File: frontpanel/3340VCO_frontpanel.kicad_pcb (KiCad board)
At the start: 2 copper layers, 20 x 128.5 mm, 0 parts

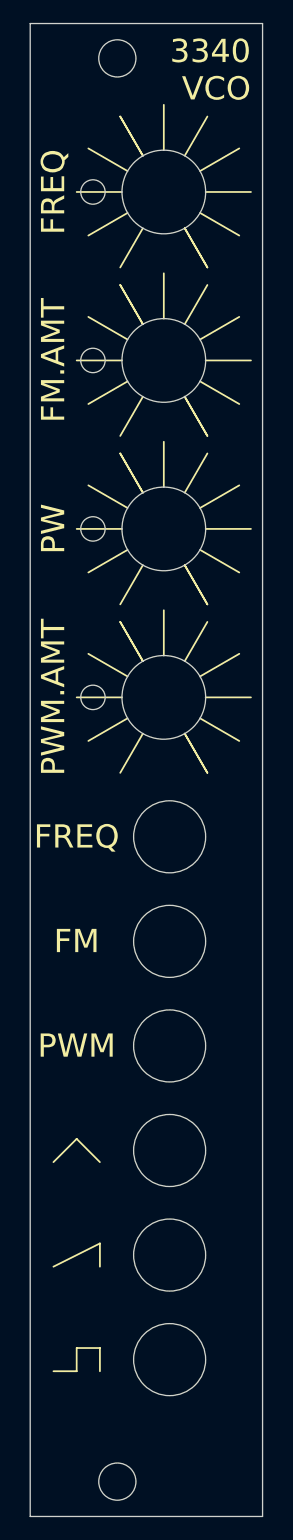
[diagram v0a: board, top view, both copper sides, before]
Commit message: tweak pcb_main, adjust frontpanel horizontal position
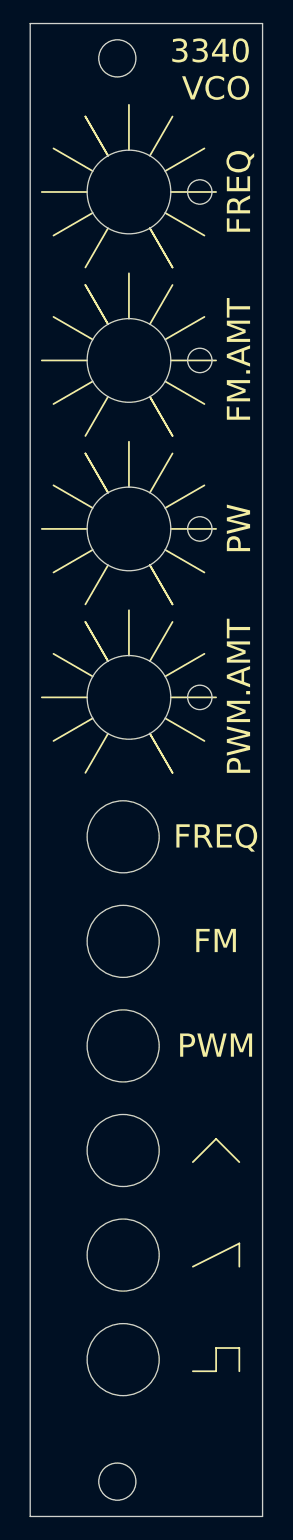
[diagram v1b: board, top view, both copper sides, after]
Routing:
- net (no net): vias 0 -> 6
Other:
- outline, holes or cut-outs redrawn

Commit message: migrate to KiCAD 6.0
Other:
- net class Default removed
